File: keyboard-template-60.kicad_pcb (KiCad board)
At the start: 2 copper layers, 285 x 95.1 mm, 169 parts, among them J1 USB_C_Receptacle_USB2.0, J2 Conn_01x04_MountingPin, SW1 SW_Reset, U1 ATmega32U4-A, U2 SRV05-4, Y1 16MHz

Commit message: Reposition the diodes, place the fuse, JST socket and reset switch
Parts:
- moved C4 278.6 mm to (18.3, 89.7)
- moved C6 229.8 mm to (-1.59, 92.1)
- moved C7 229.8 mm to (4.76, 91.3)
- moved R5 229.8 mm to (44.5, 111.9)
- moved R6 229.8 mm to (39.7, 112.7)
- moved C5 229.8 mm to (-1.72, 87.3)
- moved C8 229.8 mm to (-24.6, 89.7)
- moved R1 229.8 mm to (25.4, 103.2)
- moved R2 229.8 mm to (18.1, 110.3)
- moved R3 229.8 mm to (18.1, 118.3)
- moved R4 229.8 mm to (31.0, 127.0)
- moved C3 228.8 mm to (52.4, 112.7), turned to 180 degrees
- moved F1 214.1 mm to (94.5, 97.6)
- moved U2 208.9 mm to (102.4, 97.6), turned to 90 degrees
- moved J2 182.6 mm to (111.1, 97.6), turned to -90 degrees
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
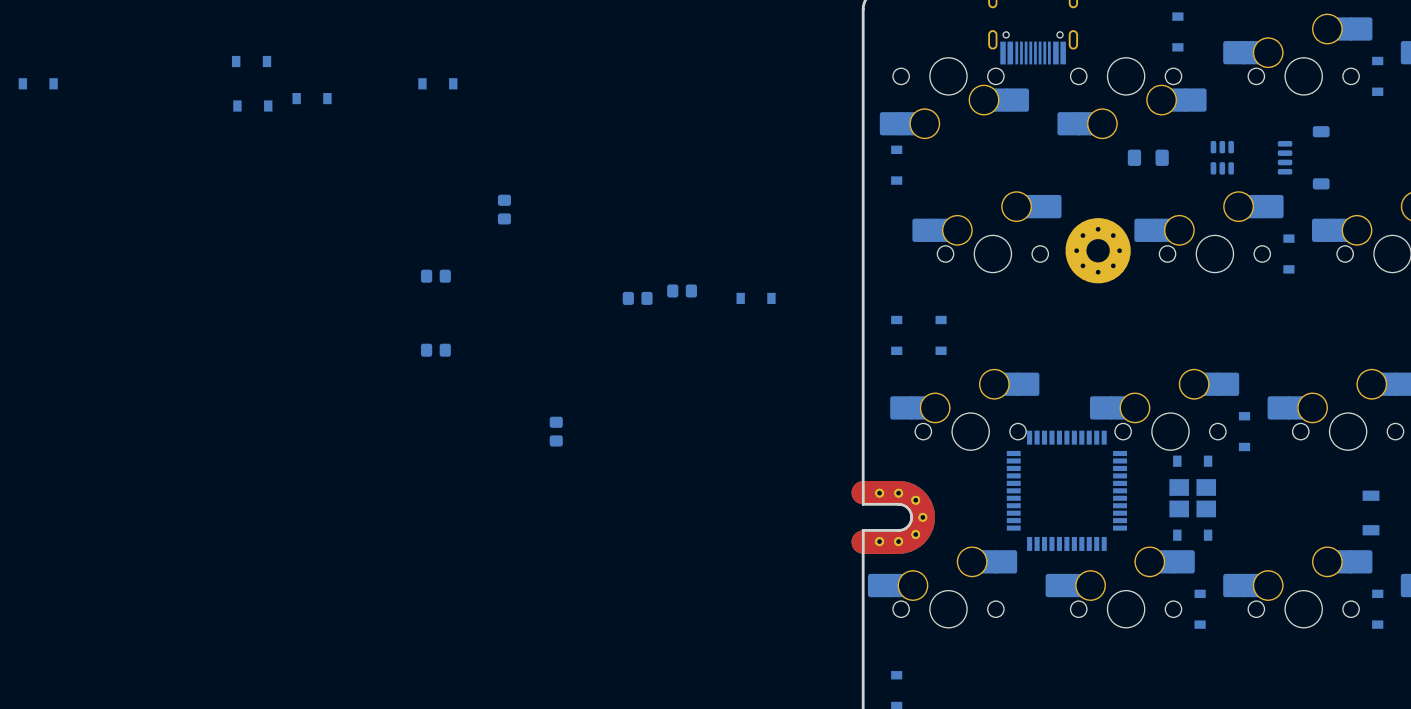
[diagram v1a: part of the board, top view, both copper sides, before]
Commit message: Further placement of components
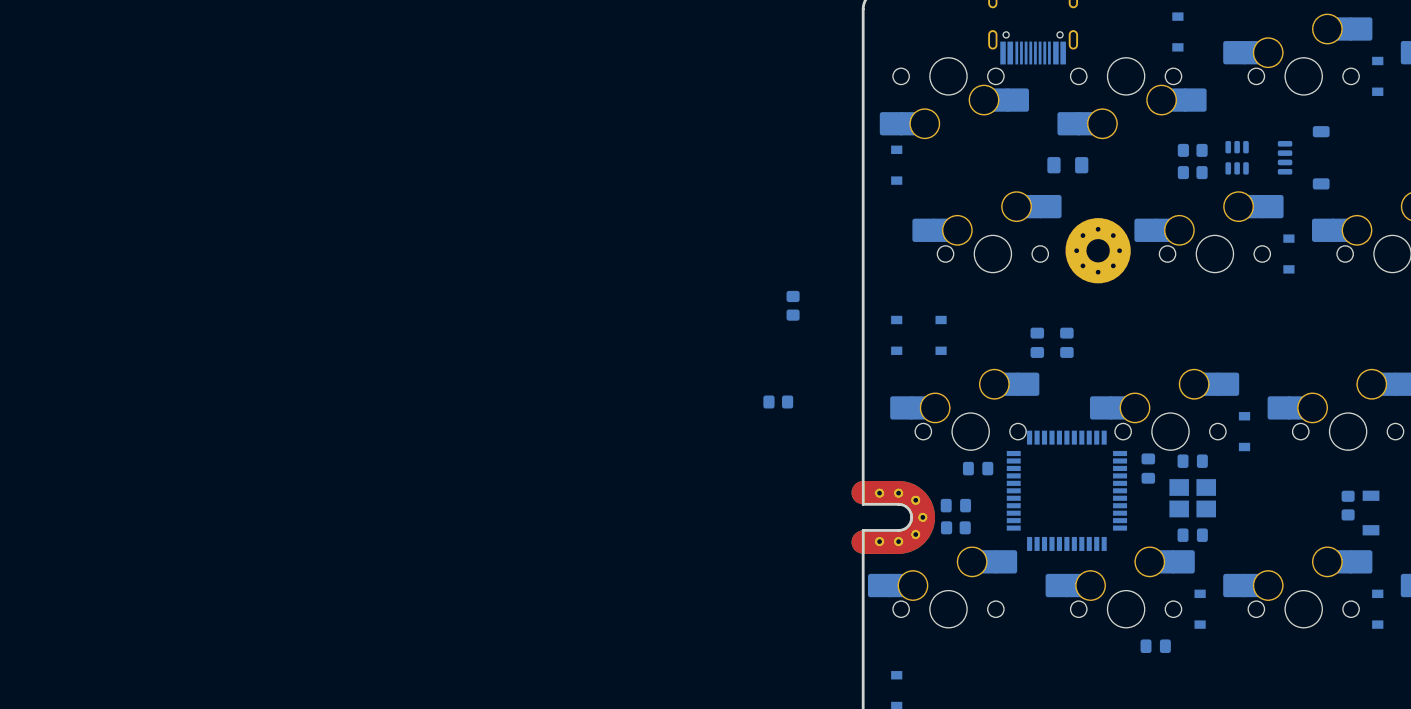
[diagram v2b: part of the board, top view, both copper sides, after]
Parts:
- C1, C2, C3, C4, C5, C6, C7, C8: footprint Diode_SMD:D_SOD-123 -> Capacitor_SMD:C_0805_2012Metric_Pad1.18x1.45mm_HandSolder
- moved C8 110.7 mm to (82.5, 117.5), turned to -90 degrees
- moved C6 103.6 mm to (94.5, 131.0), turned to -90 degrees
- moved C4 97.8 mm to (95.2, 150.0), turned to 0 degrees
- moved R1 95.9 mm to (115.9, 134.9)
- moved C5 89.3 mm to (73.8, 134.9), turned to 0 degrees
- moved C7 81.7 mm to (76.2, 131.0), turned to 0 degrees
- moved R2 62.0 mm to (73.8, 137.3)
- moved R6 61.0 mm to (99.2, 99.2)
- moved R5 56.8 mm to (99.2, 96.8)
- moved R3 37.1 mm to (54.8, 123.8)
- moved C3 33.7 mm to (85.7, 117.5), turned to -90 degrees
- moved R4 28.8 mm to (56.4, 113.5)
- moved F1 8.67 mm to (85.8, 98.4)
- moved U2 1.59 mm to (104.0, 97.6)

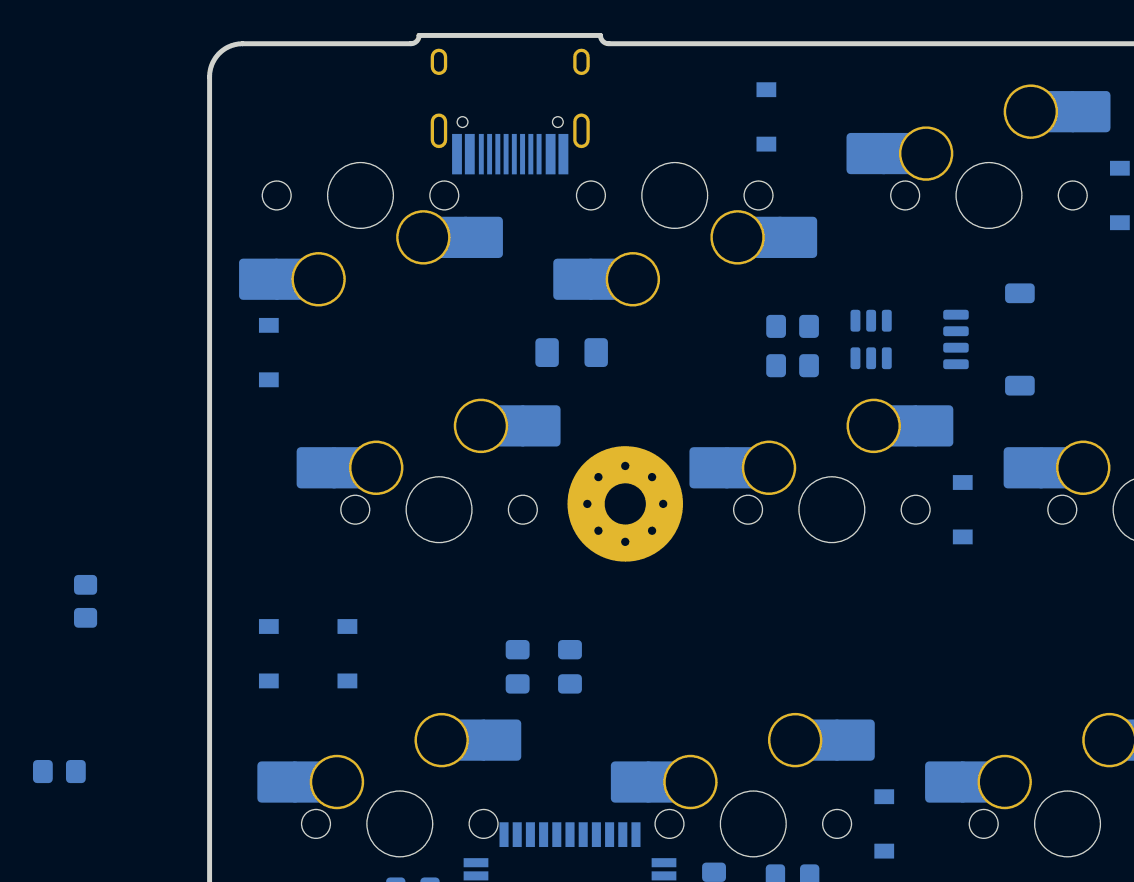
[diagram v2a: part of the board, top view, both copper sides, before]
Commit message: All parts placed, submit for checks
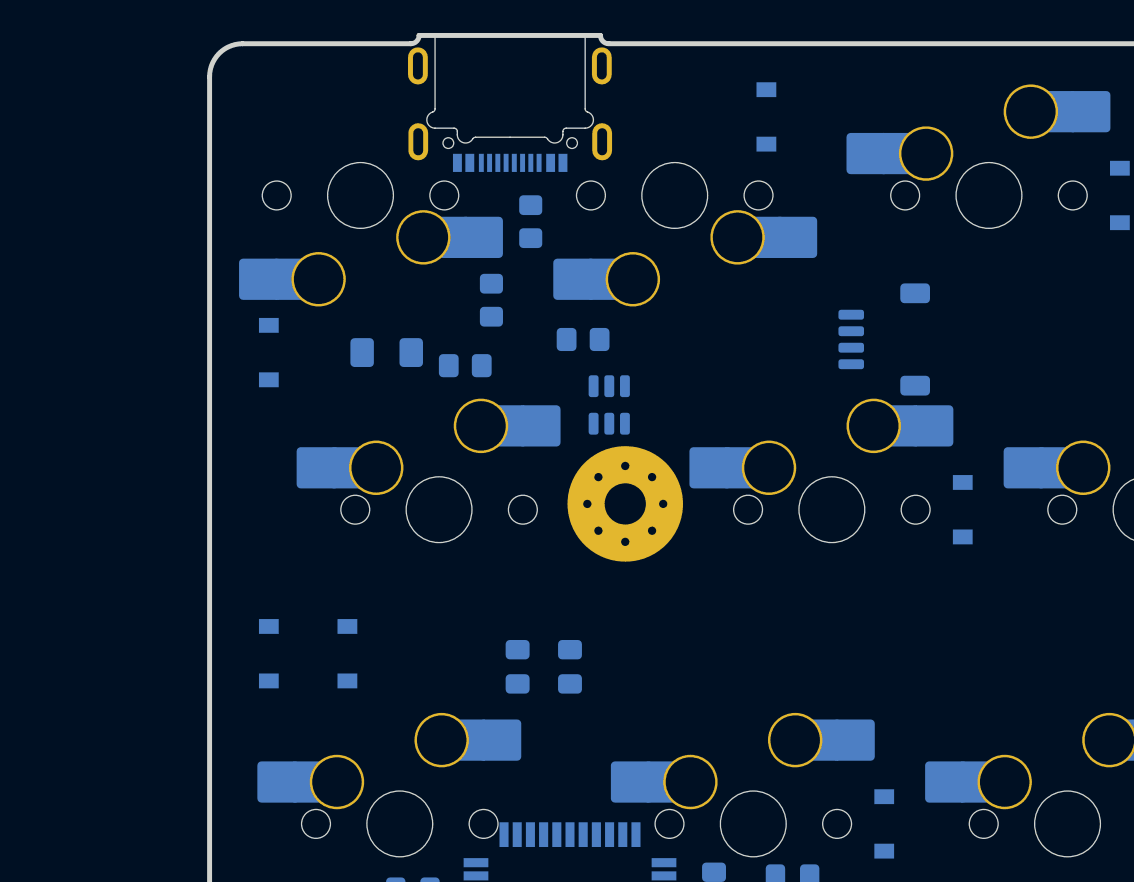
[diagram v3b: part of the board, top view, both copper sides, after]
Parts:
- J1: footprint Type-C:HRO-TYPE-C-31-M-12-HandSoldering -> marbastlib-various:USB_C_Receptacle_HRO_TYPE-C-31-M-14
- moved R3 34.8 mm to (79.4, 99.2), turned to 0 degrees
- moved R4 34.1 mm to (86.5, 97.6), turned to 0 degrees
- moved R5 18.3 mm to (81.0, 95.2), turned to -90 degrees
- moved R6 18.1 mm to (83.3, 90.5), turned to -90 degrees
- moved U2 16.4 mm to (88.1, 101.6), turned to -90 degrees
- moved F1 11.2 mm to (74.6, 98.4), turned to 0 degrees
- moved J1 7.52 mm to (82.1, 85.7)
- moved J2 6.35 mm to (104.8, 97.6)

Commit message: Fixed a bug in the schematic
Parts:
- moved C1 7.98 mm to (100.0, 138.1)
- moved C2 7.98 mm to (100.0, 130.2)
- moved Y1 0.79 mm to (100.0, 134.1)
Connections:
- net 63-2 renamed Net-(D63-Pad2)
- net 64-2 renamed Net-(D64-Pad2)
- net 65-2 renamed Net-(D65-Pad2)
- net 71-2 renamed Net-(D71-Pad2)
- net 72-2 renamed Net-(D72-Pad2)
- net 73-2 renamed Net-(D73-Pad2)
- D61 pad 1: COL10 -> ROW4
- D62 pad 1: COL10 -> ROW4
- D63 pad 1: COL10 -> ROW4
- D64 pad 1: COL10 -> ROW4
- D65 pad 1: COL10 -> ROW4
- D67 pad 1: COL10 -> ROW4
- D68 pad 1: COL10 -> ROW4
- D69 pad 1: COL10 -> ROW4
- D71 pad 1: COL10 -> ROW4
- D72 pad 1: COL10 -> ROW4
- D73 pad 1: COL10 -> ROW4
- D74 pad 1: COL10 -> ROW4
- D75 pad 1: COL10 -> ROW4
- MX12 pad 1: COL10 -> COL11
- MX13 pad 1: COL10 -> COL12
- MX18 pad 1: COL10 -> COL2
- MX19 pad 1: COL10 -> COL3
- MX20 pad 1: COL10 -> COL4
- MX27 pad 1: COL10 -> COL11
- MX28 pad 1: COL10 -> COL12
- MX3 pad 1: COL10 -> COL2
- MX33 pad 1: COL10 -> COL2
- MX34 pad 1: COL10 -> COL3
- MX35 pad 1: COL10 -> COL4
- MX4 pad 1: COL10 -> COL3
- MX42 pad 1: COL10 -> COL11
- MX43 pad 1: COL10 -> COL12
- MX48 pad 1: COL10 -> COL2
- MX49 pad 1: COL10 -> COL3
- MX5 pad 1: COL10 -> COL4
- MX50 pad 1: COL10 -> COL4
- MX57 pad 1: COL10 -> COL11
- MX58 pad 1: COL10 -> COL12
- MX63 pad 1: COL10 -> COL2
- MX64 pad 1: COL10 -> COL3
- MX65 pad 1: COL10 -> COL4
- MX72 pad 1: COL10 -> COL11
- MX73 pad 1: COL10 -> COL12
- U1 pad 12: COL10 -> COL2
- U1 pad 26: COL10 -> COL11
- U1 pad 27: COL10 -> COL12
- U1 pad 28: COL10 -> ROW4
- U1 pad 31: COL10 -> COL3
- U1 pad 32: COL10 -> COL4
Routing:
- net ROW4: track 0.00 -> 272.5 mm
- net ROW0: track 0.00 -> 260.7 mm
- net ROW2: track 0.00 -> 259.2 mm
- net ROW3: track 0.00 -> 256.4 mm
- net ROW1: track 0.00 -> 246.2 mm
- net COL6: track 0.00 -> 136.1 mm
- net COL0: track 0.00 -> 133.8 mm
- net COL8: track 0.00 -> 102.1 mm
- net COL3: track 0.00 -> 88.9 mm
- net COL13: track 0.00 -> 85.5 mm
- net COL10: track 0.00 -> 85.5 mm
- net COL11: track 0.00 -> 84.8 mm
- net COL2: track 0.00 -> 84.3 mm
- net COL4: track 0.00 -> 84.1 mm
- net COL12: track 0.00 -> 84.1 mm
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
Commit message: Start tracing
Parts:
- C1, C2, C3, C4, C5, C6, C7, C8: footprint Capacitor_SMD:C_0805_2012Metric_Pad1.18x1.45mm_HandSolder -> Capacitor_SMD:C_0603_1608Metric_Pad1.08x0.95mm_HandSolder
- R1, R2, R3, R4, R5, R6: footprint Resistor_SMD:R_0805_2012Metric_Pad1.20x1.40mm_HandSolder -> Capacitor_SMD:C_0603_1608Metric_Pad1.08x0.95mm_HandSolder
- U1: footprint Package_QFP:TQFP-44_10x10mm_P0.8mm -> Package_DFN_QFN:QFN-44-1EP_7x7mm_P0.5mm_EP5.15x5.15mm
- moved C4 12.3 mm to (92.5, 138.0)
- moved R5 8.29 mm to (88.9, 97.6)
- moved R6 8.17 mm to (87.3, 97.6)
- moved C8 8.04 mm to (83.0, 125.5), turned to 90 degrees
- moved R4 6.35 mm to (80.2, 97.6), turned to -90 degrees
- moved C1 5.46 mm to (104.5, 135.0)
- moved C2 5.30 mm to (104.5, 133.0)
- moved C5 4.80 mm to (78.5, 136.0)
- moved R2 4.73 mm to (78.5, 138.0)
- moved C7 2.50 mm to (78.5, 130.0), turned to 180 degrees
- moved C6 2.03 mm to (92.5, 131.5)
- moved R3 1.77 mm to (78.6, 97.6), turned to -90 degrees
- moved C3 0.59 mm to (86.0, 118.0), turned to 90 degrees
- turned Y1 to 90 degrees
- turned U2 to 0 degrees
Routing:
- net GND: track 0.00 -> 26.1 mm
- net +5V: track 0.33 -> 21.0 mm
- net Net-(C3-Pad1): track 0.00 -> 11.2 mm
- net Net-(R2-Pad1): track 0.00 -> 4.65 mm

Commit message: Updated the PCB outline footprint
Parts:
- moved R6 20.4 mm to (89.0, 118.0), turned to 180 degrees
- moved R5 18.4 mm to (88.5, 116.0), turned to 180 degrees
- moved R4 16.4 mm to (90.0, 84.5), turned to 90 degrees
- moved R3 13.9 mm to (74.0, 84.5), turned to 90 degrees
- moved C3 4.12 mm to (87.0, 122.0)
- moved U2 3.16 mm to (87.5, 98.5), turned to 180 degrees
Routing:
- net Net-(C3-Pad1): track 11.2 -> 0.00 mm
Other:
- outline, holes or cut-outs redrawn

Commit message: Update outline footprint, create new edge cut holes
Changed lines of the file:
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@@
     (fp_line (start -15.28125 -5.499999) (end -15.28125 7.500001) (layer "Eco2.User") (width 0.05))
     (fp_line (start 9.03125 -5.999999) (end 14.780039 -5.999999) (layer "Eco2.User") (width 0.05))
-    (fp_arc (start 9.03125 8.000001) (mid 8.677729 7.853537) (end 8.53125 7.500001) (layer "Eco2.User") (width 0.05))
+    (fp_arc (start 9.03125 8.000001) (mid 8.677693 7.853543) (end 8.53125 7.500001) (layer "Eco2.User") (width 0.05))
     (fp_arc (start -15.28125 -5.499999) (mid -15.134803 -5.853552) (end -14.78125 -5.999999) (layer "Eco2.User") (width 0.05))
     (fp_arc (start -9.03125 -5.999999) (mid -8.677697 -5.853552) (end -8.53125 -5.499999) (layer "Eco2.User") (width 0.05))
     (fp_arc (start 8.53125 -5.499999) (mid 8.677685 -5.853565) (end 9.03125 -5.999999) (layer "Eco2.User") (width 0.05))
     (fp_arc (start -8.53125 7.500001) (mid -8.677697 7.853554) (end -9.03125 8.000001) (layer "Eco2.User") (width 0.05))
-    (fp_arc (start 14.780039 -5.999999) (mid 15.133567 -5.853539) (end 15.280039 -5.499999) (layer "Eco2.User") (width 0.05))
-    (fp_arc (start 15.28125 7.500001) (mid 15.134806 7.853571) (end 14.78125 8.000001) (layer "Eco2.User") (width 0.05))
+    (fp_arc (start 14.780039 -5.999999) (mid 15.133602 -5.853545) (end 15.280039 -5.499999) (layer "Eco2.User") (width 0.05))
+    (fp_arc (start 15.28125 7.500001) (mid 15.1348 7.853536) (end 14.78125 8.000001) (layer "Eco2.User") (width 0.05))
     (fp_arc (start -14.78125 8.000001) (mid -15.134803 7.853554) (end -15.28125 7.500001) (layer "Eco2.User") (width 0.05))
     (fp_circle (center 11.90625 -6.985) (end 13.90625 -6.985) (layer "B.CrtYd") (width 0.12) (fill none))
@@
     (fp_line (start -15.28125 -5.499999) (end -15.28125 7.500001) (layer "Eco2.User") (width 0.05))
     (fp_line (start -14.78125 8.000001) (end -9.03125 8.000001) (layer "Eco2.User") (width 0.05))
-    (fp_arc (start 15.28125 7.500001) (mid 15.134806 7.853571) (end 14.78125 8.000001) (layer "Eco2.User") (width 0.05))
+    (fp_arc (start 15.28125 7.500001) (mid 15.1348 7.853536) (end 14.78125 8.000001) (layer "Eco2.User") (width 0.05))
     (fp_arc (start -15.28125 -5.499999) (mid -15.134803 -5.853552) (end -14.78125 -5.999999) (layer "Eco2.User") (width 0.05))
     (fp_arc (start -14.78125 8.000001) (mid -15.134803 7.853554) (end -15.28125 7.500001) (layer "Eco2.User") (width 0.05))
     (fp_arc (start -9.03125 -5.999999) (mid -8.677697 -5.853552) (end -8.53125 -5.499999) (layer "Eco2.User") (width 0.05))
-    (fp_arc (start 14.780039 -5.999999) (mid 15.133567 -5.853539) (end 15.280039 -5.499999) (layer "Eco2.User") (width 0.05))
-    (fp_arc (start 9.03125 8.000001) (mid 8.677729 7.853537) (end 8.53125 7.500001) (layer "Eco2.User") (width 0.05))
+    (fp_arc (start 14.780039 -5.999999) (mid 15.133602 -5.853545) (end 15.280039 -5.499999) (layer "Eco2.User") (width 0.05))
+    (fp_arc (start 9.03125 8.000001) (mid 8.677693 7.853543) (end 8.53125 7.500001) (layer "Eco2.User") (width 0.05))
     (fp_arc (start 8.53125 -5.499999) (mid 8.677685 -5.853565) (end 9.03125 -5.999999) (layer "Eco2.User") (width 0.05))
     (fp_arc (start -8.53125 7.500001) (mid -8.677697 7.853554) (end -9.03125 8.000001) (layer "Eco2.User") (width 0.05))
@@
     (fp_arc (start -138.7 7.8) (mid -137.710051 8.210051) (end -137.3 9.2) (layer "Edge.Cuts") (width 0.3))
     (fp_arc (start -142.5 -45.3) (mid -141.914214 -46.714214) (end -140.5 -47.3) (layer "Edge.Cuts") (width 0.3))
-    (pad "1" thru_hole oval locked (at 117.3 -19.4) (size 5 3) (drill oval 4.5 2.49936) (layers *.Cu *.Mask))
+    (pad "1" thru_hole oval locked (at 117.3 -19.4) (size 4.8 2.8) (drill oval 4.5 2.49936) (layers *.Cu *.Mask))
     (pad "1" thru_hole oval locked (at -141 9.2) (size 8 3.5) (drill oval 7.00126 2.49936) (layers *.Cu *.Mask))
     (pad "1" thru_hole oval locked (at 140.9 9.2) (size 8 3.5) (drill oval 7.00126 2.49936) (layers *.Cu *.Mask))
-    (pad "1" thru_hole oval locked (at 48 37.9) (size 5.5 3) (drill oval 5.00126 2.49936) (layers *.Cu *.Mask))
-    (pad "1" thru_hole circle locked (at -117.3 -19.4) (size 2.6 2.6) (drill 2.4994) (layers *.Cu *.Mask))
+    (pad "1" thru_hole circle locked (at -117.3 -19.4) (size 2.8 2.8) (drill 2.4994) (layers *.Cu *.Mask))
   )
   (footprint "marbastlib-mx:SW_MX_HS_1u" (layer "B.Cu")
@@
     (fp_arc (start 4.687858 -1.884158) (mid 4.584652 -1.9563) (end 4.545001 -2.075821) (layer "Edge.Cuts") (width 0.08))
     (fp_arc (start 3.195001 -0.705) (mid 3.253579 -0.846421) (end 3.395 -0.904999) (layer "Edge.Cuts") (width 0.08))
-    (fp_arc (start 2.088783 -0.355) (mid 2.188776 -0.328203) (end 2.261988 -0.255) (layer "Edge.Cuts") (width 0.08))
+    (fp_arc (start 2.088783 -0.355) (mid 2.188789 -0.328211) (end 2.261988 -0.255) (layer "Edge.Cuts") (width 0.08))
     (fp_arc (start -2.271986 -0.255) (mid -2.198781 -0.328205) (end -2.098781 -0.355) (layer "Edge.Cuts") (width 0.08))
     (fp_line (start 4.465 1.045) (end 4.465001 -6.915) (layer "B.CrtYd") (width 0.08))
@@
     )
   )
+  (gr_arc (start 253.1 166.2) (mid 251.8 164.9) (end 253.1 163.6) (layer "Edge.Cuts") (width 0.2))
+  (gr_arc (start 255.6 163.6) (mid 256.9 164.9) (end 255.6 166.2) (layer "Edge.Cuts") (width 0.2))
+  (gr_line (start 253.1 166.2) (end 255.6 166.2) (layer "Edge.Cuts") (width 0.2))
+  (gr_line (start 255.6 163.6) (end 253.05 163.6) (layer "Edge.Cuts") (width 0.2))
   (segment (start 82.2875 131.35) (end 78.9875 131.35) (width 0.381) (layer "B.Cu") (net 1))
   (segment (start 81.65 135.35) (end 81 136) (width 0.381) (layer "B.Cu") (net 1))

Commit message: Final traces, first draft.
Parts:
- moved D1 31.2 mm to (95.2, 84.1)
- moved D16 27.9 mm to (95.2, 114.3)
- moved D31 20.0 mm to (92.1, 114.3)
- moved D46 19.6 mm to (86.5, 150.0)
- moved F1 15.4 mm to (89.5, 102.1)
- moved D30 9.82 mm to (342.9, 108.0)
- moved R6 5.20 mm to (85.3, 114.3), turned to -90 degrees
- moved R5 5.08 mm to (83.7, 114.3), turned to -90 degrees
- moved D37 4.76 mm to (204.8, 121.4)
- moved D39 4.76 mm to (208.0, 121.4)
- moved C6 3.99 mm to (96.3, 132.6)
- moved R1 3.57 mm to (114.3, 131.8), turned to 180 degrees
- moved D45 3.18 mm to (345.3, 127.0)
- moved C3 2.91 mm to (85.7, 124.6), turned to -90 degrees
- moved SW1 2.38 mm to (121.4, 133.3)
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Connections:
- J1 pad A6: Net-(J1-PadA6) -> D+
- J1 pad A7: Net-(J1-PadA7) -> D-
- J1 pad B6: Net-(J1-PadA6) -> D+
- J1 pad B7: Net-(J1-PadA7) -> D-
- R5 pad 1: Net-(J1-PadA7) -> D-
- R5 pad 2: D- -> Net-(R5-Pad2)
- R6 pad 1: Net-(J1-PadA6) -> D+
- R6 pad 2: D+ -> Net-(R6-Pad2)
- U1 pad 1: COL13 -> COL0
- U1 pad 10: ROW2 -> unconnected-(U1-Pad10)
- U1 pad 11: ROW3 -> unconnected-(U1-Pad11)
- U1 pad 12: COL2 -> ROW2
- U1 pad 18: COL5 -> unconnected-(U1-Pad18)
- U1 pad 19: COL6 -> COL9
- U1 pad 20: COL7 -> COL5
- U1 pad 21: COL8 -> COL4
- U1 pad 22: COL10 -> COL3
- U1 pad 25: COL9 -> ROW3
- U1 pad 26: COL11 -> COL14
- U1 pad 27: COL12 -> COL13
- U1 pad 28: ROW4 -> COL12
- U1 pad 29: COL0 -> COL11
- U1 pad 3: D- -> Net-(R5-Pad2)
- U1 pad 30: COL1 -> COL10
- U1 pad 31: COL3 -> COL8
- U1 pad 32: COL4 -> COL7
- U1 pad 36: unconnected-(U1-Pad36) -> COL6
- U1 pad 37: unconnected-(U1-Pad37) -> COL2
- U1 pad 38: unconnected-(U1-Pad38) -> COL1
- U1 pad 39: unconnected-(U1-Pad39) -> ROW4
- U1 pad 4: D+ -> Net-(R6-Pad2)
- U1 pad 41: COL14 -> unconnected-(U1-Pad41)
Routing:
- net COL14: track 80.1 -> 358.8 mm
- net COL13: track 85.5 -> 345.2 mm
- net COL12: track 84.1 -> 325.2 mm
- net COL11: track 84.8 -> 306.9 mm
- net COL10: track 85.5 -> 285.5 mm
- net COL8: track 102.1 -> 276.3 mm
- net COL9: track 65.0 -> 216.8 mm
- net COL7: track 76.7 -> 220.2 mm
- net COL6: track 136.1 -> 241.8 mm
- net +5V: track 21.0 -> 116.9 mm, vias 0 -> 6
- net COL1: track 77.2 -> 160.5 mm
- net GND: track 26.1 -> 104.7 mm, vias 0 -> 6
- net COL5: track 65.0 -> 140.4 mm
- net ROW0: track 260.7 -> 329.0 mm
- net D-: track 0.00 -> 67.9 mm
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- added copper zone on B.Cu, net GND
